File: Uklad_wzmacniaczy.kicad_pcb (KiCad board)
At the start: 4 copper layers, 80.6 x 107 mm, 81 parts, among them J1 MEM2080-00-128-00-A, J2 SJ1-3523N, U1 OPA2388IDR, U10 LD1117S50TR_SOT223, U11 LT3094EMSE-TRPBF, U12 NUCLEO-H755ZIQ, U2 REF2033QDDCRQ1, U3 AD8421ARMZ, U4 OPA388IDR, U5 AD8421ARMZ, U6 TPD4E1B06DRLR, U7 LT3042EMSE-TRPBF, U8 TPS65135RTER, U9 TPS61236PRWLR

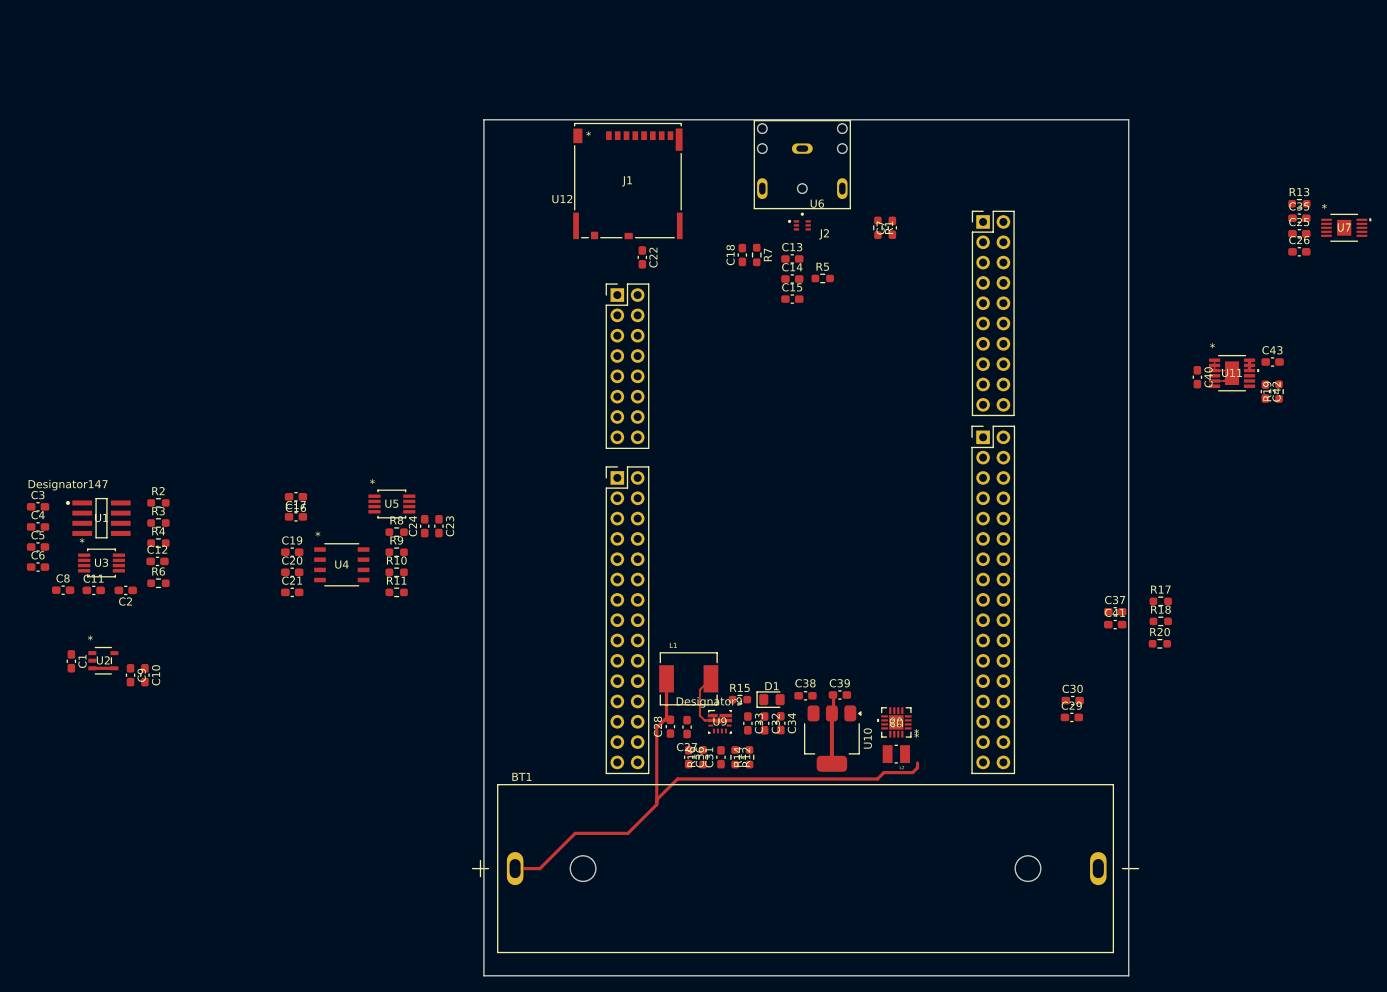
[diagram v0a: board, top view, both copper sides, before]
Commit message: Schematic minor change Vbat -> 3.3V, PCB layout: +5V, -5V
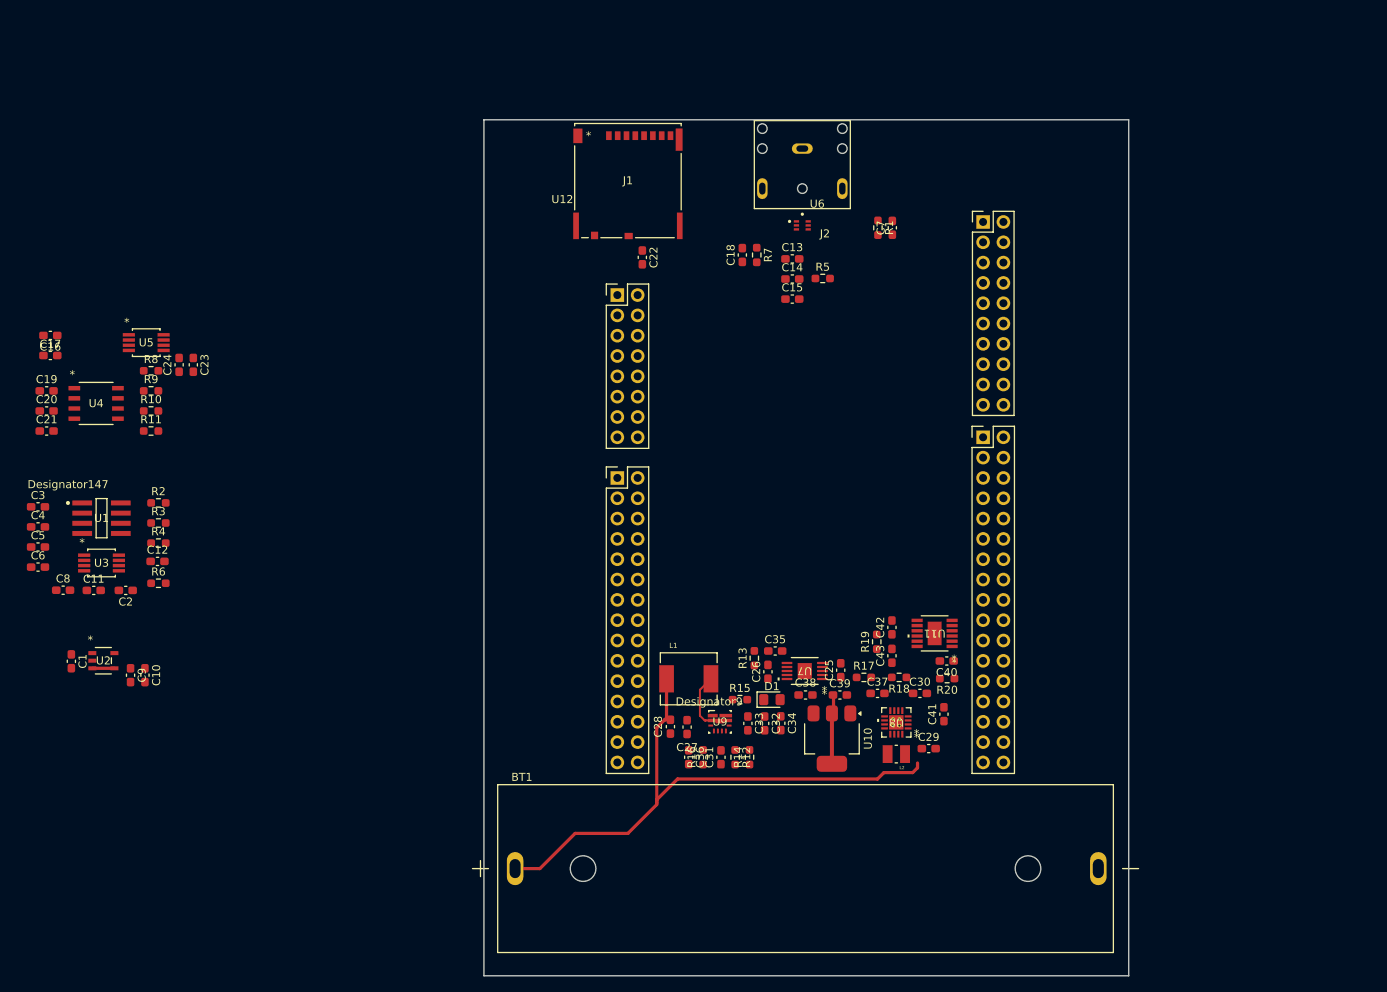
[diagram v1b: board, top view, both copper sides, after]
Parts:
- moved R13 88.7 mm to (139.4, 103.1), turned to 90 degrees
- moved U7 87.3 mm to (145.7, 104.7), turned to 180 degrees
- moved C35 85.0 mm to (142.0, 102.2)
- moved C26 84.7 mm to (141.1, 104.8), turned to 90 degrees
- moved C25 79.1 mm to (150.2, 104.6), turned to 90 degrees
- moved C43 60.1 mm to (156.6, 102.8), turned to 90 degrees
- moved R19 59.2 mm to (154.7, 101.0)
- moved C42 55.2 mm to (156.6, 99.2), turned to 90 degrees
- moved U11 49.4 mm to (161.9, 100.0), turned to 180 degrees
- moved C40 47.3 mm to (163.4, 103.5), turned to 180 degrees
- moved R17 38.3 mm to (153.1, 105.5)
- moved R10 36.7 mm to (64.0, 72.2)
- moved R11 36.7 mm to (64.0, 74.7)
- moved R8 36.7 mm to (64.0, 67.2)
- moved R9 36.7 mm to (64.0, 69.7)
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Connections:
- U8 pad 8: +BATT -> +3.3V
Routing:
- net /OUTN: track 6.21 -> 0.00 mm
- net -5VA: track 1.30 -> 0.00 mm

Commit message: New STM footprint, changed PCB layout, added pin connector
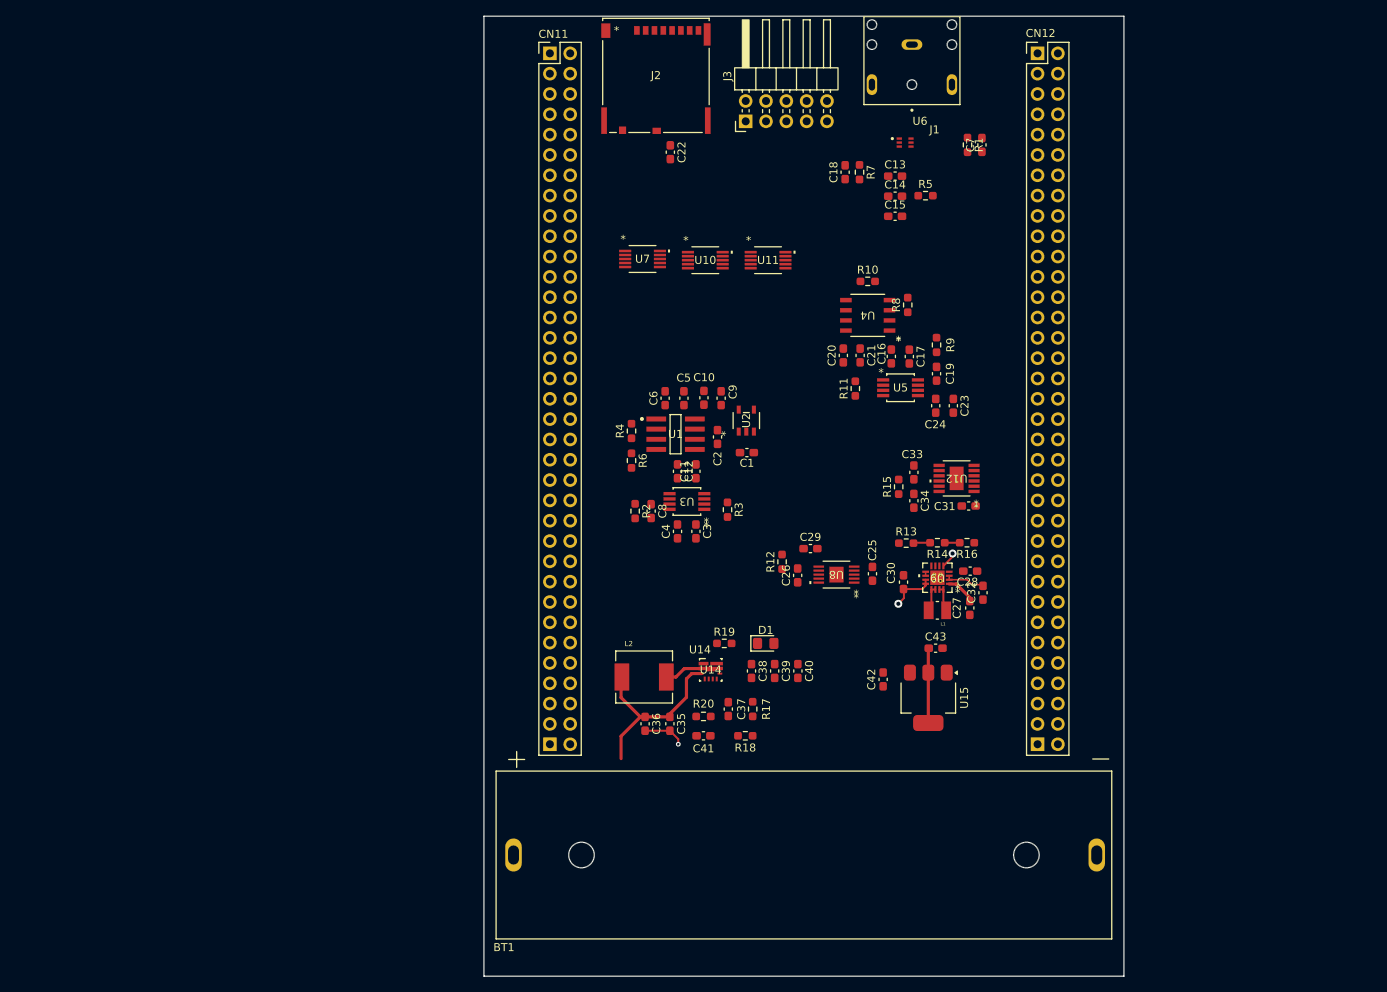
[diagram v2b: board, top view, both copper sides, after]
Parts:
- removed the C27 at (131.0, 111.7)
- removed the C28 at (128.9, 111.7)
- removed the C31 at (135.2, 115.5)
- removed the C32 at (140.7, 111.2)
- removed the C33 at (138.6, 111.2)
- removed the C34 at (142.7, 111.2)
- removed the L1 at (131.2, 105.7)
- removed the R12 at (137.0, 115.5)
- removed the R14 at (138.8, 115.5)
- removed the R15 at (137.6, 108.3)
- removed the R16 at (133.0, 115.5)
- removed the U12 at (121.0, 47.0)
- removed the U9 at (135.1, 111.0)
- added C35: 10u, Capacitor_SMD:C_0603_1608Metric_Pad1.08x0.95mm_HandSolder, F.Cu at (128.8, 111.3)
- added C37: 10p, Capacitor_SMD:C_0603_1608Metric_Pad1.08x0.95mm_HandSolder, F.Cu at (136.1, 109.5)
- added C40: 22u, Capacitor_SMD:C_0603_1608Metric_Pad1.08x0.95mm_HandSolder, F.Cu at (144.8, 104.7)
- added C41: 10n, Capacitor_SMD:C_0603_1608Metric_Pad1.08x0.95mm_HandSolder, F.Cu at (133.0, 112.8)
- added C42: 10u, Capacitor_SMD:C_0603_1608Metric_Pad1.08x0.95mm_HandSolder, F.Cu at (155.5, 105.8)
- added C43: 10u, Capacitor_SMD:C_0603_1608Metric_Pad1.08x0.95mm_HandSolder, F.Cu at (162.1, 101.8)
- added J3: Conn_01x10_Pin, Connector_PinHeader_2.54mm:PinHeader_2x05_P2.54mm_Horizontal, F.Cu at (138.3, 36.0)
- added L2: 1u, Uklad_wzmacniaczy_footprints:IND_SPM6530T-1R0M120, F.Cu at (125.6, 105.5)
- added R17: 1M, Resistor_SMD:R_0603_1608Metric_Pad0.98x0.95mm_HandSolder, F.Cu at (139.2, 109.5)
- added R18: 332k, Resistor_SMD:R_0603_1608Metric_Pad0.98x0.95mm_HandSolder, F.Cu at (138.3, 112.8)
- added R19: 2k, Resistor_SMD:R_0603_1608Metric_Pad0.98x0.95mm_HandSolder, F.Cu at (135.6, 101.2)
- added R20: 41.2k, Resistor_SMD:R_0603_1608Metric_Pad0.98x0.95mm_HandSolder, F.Cu at (133.0, 110.4)
- added U11: AD5162BRMZ10-RL7, Uklad_wzmacniaczy_footprints:RM_10_ADI, F.Cu at (141.1, 53.3)
- added U13: Nucleo-H755ZIQ-Morpho, Uklad_wzmacniaczy_footprints:Nucleo-H755ZIQ-Morpho, F.Cu at (146.9, 70.7)
- added U14: TPS61236PRWLR, Uklad_wzmacniaczy_footprints:RWL0009A, F.Cu at (133.9, 104.5)
- added U15: LD1117S50TR_SOT223, Package_TO_SOT_SMD:SOT-223-3_TabPin2, F.Cu at (161.2, 108.0)
- added U7: AD5162BRMZ10-RL7, Uklad_wzmacniaczy_footprints:RM_10_ADI, F.Cu at (125.4, 53.2)
- C36: value 10n -> 1u
- C38, C39: value 10u -> 22u
- U10: value LD1117S50TR_SOT223 -> AD5162BRMZ10-RL7; footprint Package_TO_SOT_SMD:SOT-223-3_TabPin2 -> Uklad_wzmacniaczy_footprints:RM_10_ADI
- moved C19 111.3 mm to (162.2, 67.5), turned to 90 degrees
- moved C17 107.4 mm to (158.8, 65.4), turned to -90 degrees
- moved C16 105.2 mm to (156.5, 65.4), turned to 90 degrees
- moved C21 102.1 mm to (152.6, 65.3), turned to -90 degrees
- moved C20 99.8 mm to (150.5, 65.3), turned to 90 degrees
- moved R9 98.4 mm to (162.2, 63.9), turned to 90 degrees
- moved U4 97.1 mm to (153.6, 60.2), turned to 180 degrees
- moved C23 95.1 mm to (164.3, 71.5)
- moved R8 94.9 mm to (158.6, 58.9), turned to 90 degrees
- moved C24 94.7 mm to (162.1, 71.5)
- moved U5 94.5 mm to (157.7, 69.3)
- moved R10 91.0 mm to (153.6, 56.0)
- moved C1 88.4 mm to (138.5, 77.4), turned to 0 degrees
- moved R11 88.2 mm to (152.0, 69.4), turned to 90 degrees
- moved U2 85.8 mm to (138.4, 73.4), turned to 90 degrees
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- renumbered C29 to C27, C30 to C28, C35 to C29, C37 to C30, C40 to C31, C41 to C32, C42 to C33, C43 to C34, J2 to J1, J1 to J2, L2 to L1, R13 to R12, R17 to R13, R18 to R14, R19 to R15, R20 to R16, U11 to U12, U7 to U8, U8 to U9
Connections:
- C1 pad 2: GND -> GNDA
- C10 pad 2: GND -> GNDA
- C11 pad 2: GND -> GNDA
- C12 pad 1: GND -> GNDA
- C13 pad 2: GND -> GNDA
- C16 pad 2: GND -> GNDA
- C17 pad 1: GND -> GNDA
- C18 pad 2: GND -> GNDA
- C2 pad 2: GND -> GNDA
- C20 pad 1: GND -> GNDA
- C21 pad 2: GND -> GNDA
- C23 pad 2: GND -> GNDA
- C24 pad 1: GND -> GNDA
- C25 pad 2: GND -> GNDA
- C26 pad 2: GND -> GNDA
- C27 pad 2: GND -> GNDA
- C28 pad 1: GND -> GNDA
- C29 pad 2: GND -> GNDA
- C3 pad 2: GND -> GNDA
- C30 pad 2: GND -> GNDA
- C31 pad 2: GND -> GNDA
- C32 pad 1: GND -> GNDA
- C33 pad 2: GND -> GNDA
- C34 pad 2: GND -> GNDA
- C36 pad 1: /CC -> +BATT
- C39 pad 1: +3.3V -> +5V
- C4 pad 1: GND -> GNDA
- C5 pad 1: GND -> GNDA
- C6 pad 2: GND -> GNDA
- C7 pad 2: GND -> GNDA
- C9 pad 2: GND -> GNDA
- R12 pad 1: GND -> GNDA
- R15 pad 1: GND -> GNDA
- U1 pad 4: GND -> GNDA
- U10 pad 1: GND -> GNDA
- U10 pad 2: +3.3V -> unconnected-(U10-A1-Pad2)
- U10 pad 3: +5V -> /SIG_4
- U12 pad 6: GND -> GNDA
- U12 pad 9: GND -> GNDA
- U2 pad 2: GND -> GNDA
- U3 pad 6: GND -> GNDA
- U4 pad 4: GND -> GNDA
- U5 pad 6: GND -> GNDA
- U6 pad 2: GND -> GNDA
- U8 pad 5: GND -> GNDA
- U8 pad 8: GND -> GNDA
- U9 pad 11: GND -> GNDA
- U9 pad 12: GND -> GNDA
- U9 pad 5: GND -> GNDA
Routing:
- net +BATT: track 73.2 -> 27.6 mm
- net GNDA: track 0.00 -> 7.86 mm, vias 0 -> 2
- net Net-(U9-SW): track 7.03 -> 0.00 mm
- net GND: track 0.00 -> 5.22 mm, vias 0 -> 1
- net /OUTN: track 0.00 -> 5.04 mm
- net Net-(U14-SW): track 0.00 -> 4.83 mm
- net Net-(L1-Pad1): track 0.00 -> 3.24 mm
- net Net-(L1-Pad2): track 0.00 -> 3.24 mm
- net +5VA: track 2.76 -> 0.00 mm
- net /FB: track 0.00 -> 2.10 mm
- net /FBG: track 0.00 -> 1.88 mm
- net +3.3V: track 8.62 -> 9.37 mm
- net /OUTP: track 0.00 -> 0.50 mm
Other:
- board size 80.6 x 107 mm -> 80 x 120 mm

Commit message: Nucleo-shield pins change
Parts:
- moved R3 27.5 mm to (138.3, 57.1)
- moved U3 26.3 mm to (132.1, 57.2)
- moved C11 26.3 mm to (133.2, 53.4)
- moved C12 26.3 mm to (130.9, 53.4)
- moved C3 26.3 mm to (133.2, 61.0)
- moved C4 26.3 mm to (130.9, 61.0)
- moved C8 23.8 mm to (127.0, 61.0)
- moved R6 13.6 mm to (127.3, 65.2), turned to 90 degrees
- moved R2 13.4 mm to (128.2, 71.8), turned to 90 degrees
- moved C6 12.1 mm to (139.1, 65.2)
- moved R4 10.8 mm to (129.2, 65.2)
- moved C5 8.14 mm to (136.7, 65.2)
- moved C2 6.55 mm to (139.1, 70.5)
- moved U1 6.44 mm to (133.8, 70.2)
- moved C13 6.44 mm to (151.6, 46.4)
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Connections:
- U13 pad 1.04: /Nucleo/SDMMC_CMD -> /SDMMC_CMD
- U13 pad 1.13: unconnected-(U13-PA13-Pad1.13) -> /DETECT_SD
- U13 pad 1.45: unconnected-(U13-PD7-Pad1.45) -> /SDI
- U13 pad 2.11: unconnected-(U13-PA5-Pad2.11) -> /CLK
- U13 pad 2.13: unconnected-(U13-PA6-Pad2.13) -> /Nucleo/SPI_MISO
- U13 pad 2.16: unconnected-(U13-PB12-Pad2.16) -> /CS_2
- U13 pad 2.17: unconnected-(U13-PB6-Pad2.17) -> /CS_1
- U13 pad 2.18: unconnected-(U13-PB11-Pad2.18) -> /CS_3
- U13 pad 2.37: unconnected-(U13-PA3-Pad2.37) -> /SIG_6
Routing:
- net /SDMMC_D0: track 0.00 -> 52.0 mm
- net GNDA: track 7.86 -> 55.6 mm, vias 2 -> 7
- net /SDMMC_D1: track 0.00 -> 47.5 mm
- net GND: track 5.22 -> 41.6 mm, vias 1 -> 10
- net +3.3V: track 9.37 -> 32.6 mm, vias 0 -> 3
- net /SDMMC_CK: track 0.00 -> 20.8 mm
- net /TO_ADC1: track 0.00 -> 20.4 mm, vias 0 -> 1
- net /Reference_In: track 0.00 -> 17.8 mm
- net +5V: track 0.00 -> 17.7 mm
- net +5VA: track 0.00 -> 15.9 mm
- net /Analog_In1: track 0.00 -> 14.5 mm
- net Net-(U1A-+IN_A): track 0.00 -> 14.5 mm
- net /SDMMC_CMD: track 0.00 -> 14.5 mm
- net /Analog_In2: track 0.00 -> 13.5 mm
- net /SDMMC_D2: track 0.00 -> 12.7 mm
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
